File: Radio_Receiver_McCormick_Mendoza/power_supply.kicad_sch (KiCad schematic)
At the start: 31 parts, among them J1 VBAT, J2 GND, J23 VDDA, J26 +5V, J3 VA_3.3, J36 +5V RAW, J37 V_4.5, J39 VDD, J4 VA_4.5, J6 Conn_01x02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

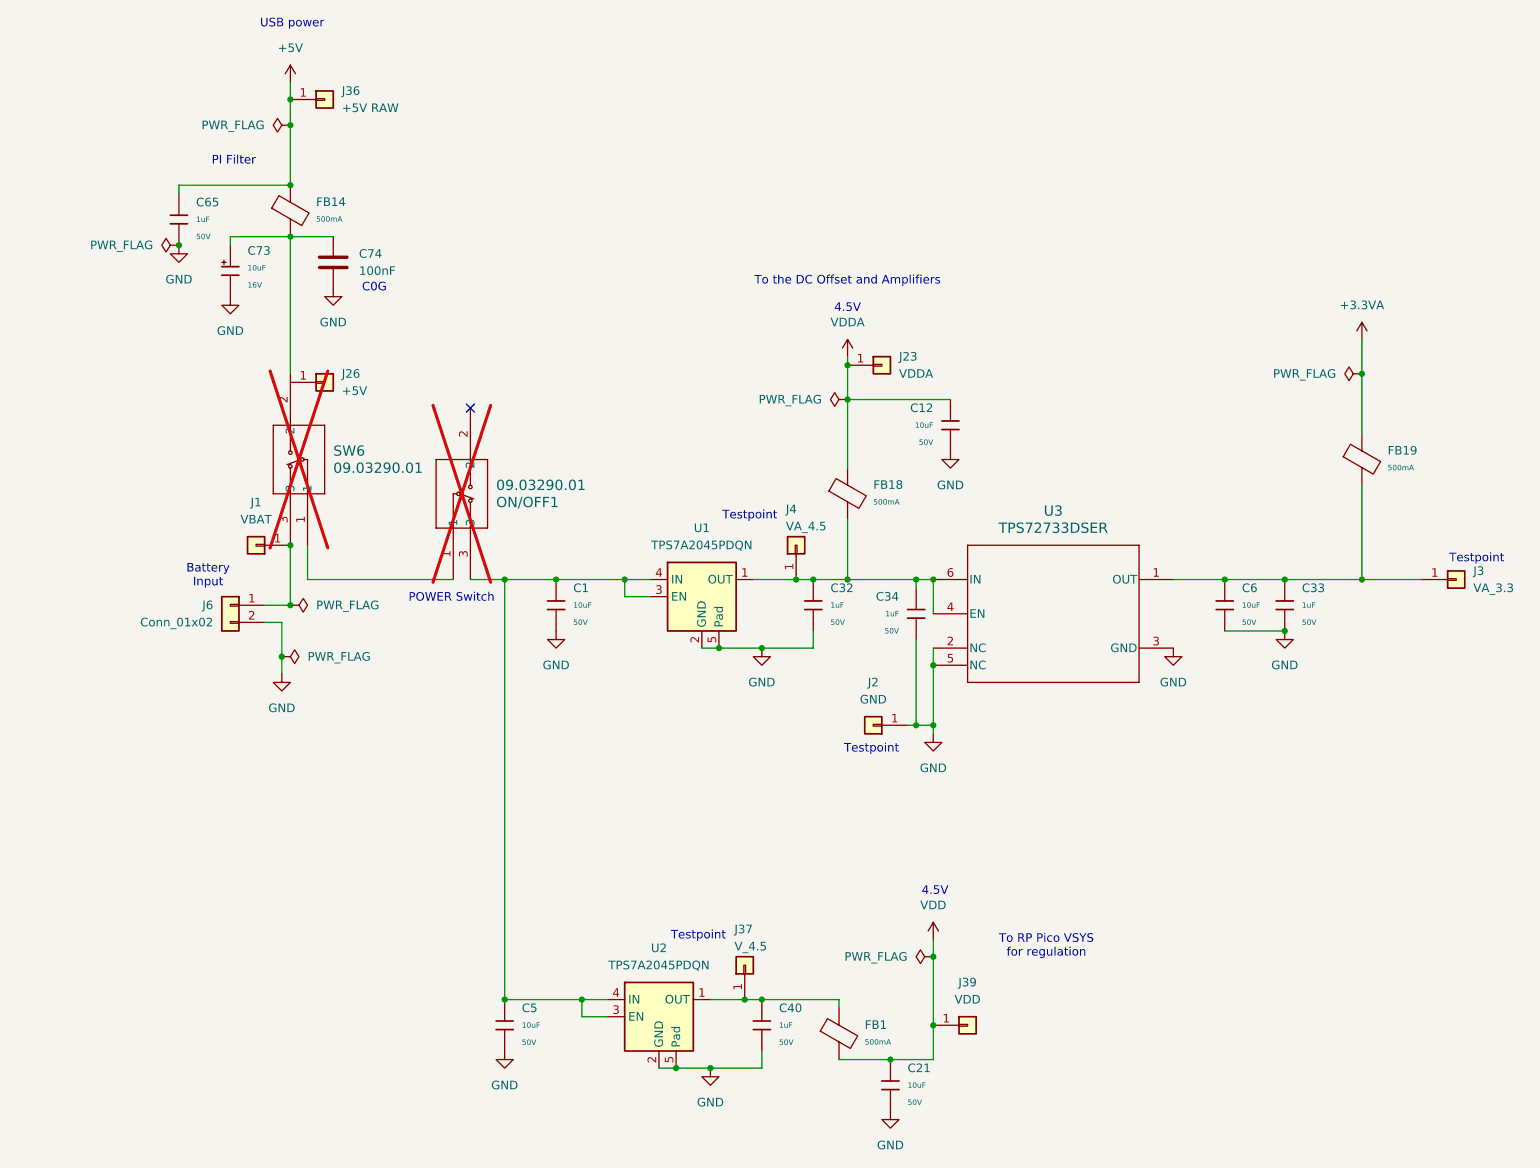
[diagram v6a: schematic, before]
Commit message: Arranged power components on PCB
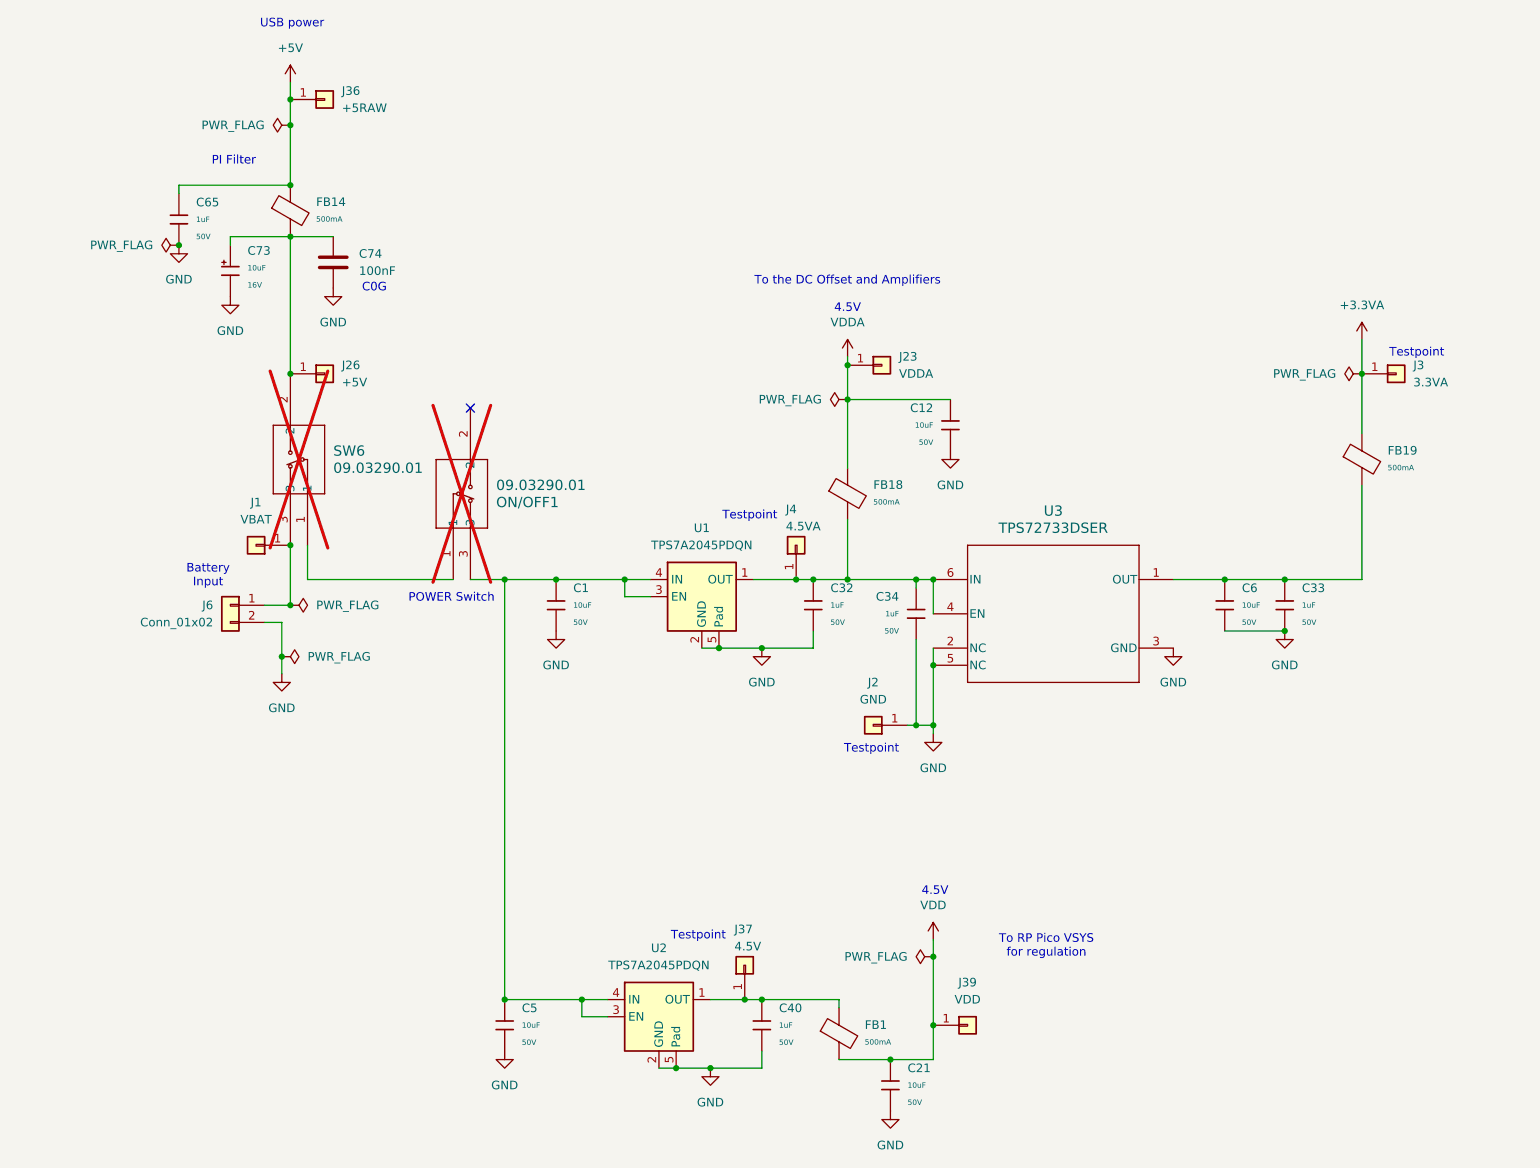
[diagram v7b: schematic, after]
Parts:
- J3: value VA_3.3 -> 3.3VA
- J36: value +5V RAW -> +5RAW
- J37: value V_4.5 -> 4.5V
- J4: value VA_4.5 -> 4.5VA
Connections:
- net +3.3VA: now also J3.1 (Pin_1)
- net at C73.1, C74.1, FB14.2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: now also J26.1 (Pin_1)
- net at C33.1, C6.1, FB19.2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: no longer J3.1 (Pin_1)
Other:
- moved on the sheet: J26, J3
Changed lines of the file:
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@@
 	(text "Testpoint"
 		(exclude_from_sim no)
-		(at 235.458 98.552 0)
+		(at 226.568 68.072 0)
 		(effects
 			(font
@@
 	)
 	(junction
-		(at 218.44 101.6)
-		(diameter 0)
-		(color 0 0 0 0)
-	)
-	(junction
 		(at 59.69 105.41)
 		(diameter 0)
@@
 	)
 	(junction
+		(at 59.69 71.12)
+		(diameter 0)
+		(color 0 0 0 0)
+	)
+	(junction
 		(at 59.69 34.29)
 		(diameter 0)
@@
 	(wire
 		(pts
-			(xy 218.44 101.6) (xy 227.33 101.6)
-		)
-		(stroke
-			(width 0)
-			(type default)
-		)
-	)
-	(wire
-		(pts
 			(xy 154.94 101.6) (xy 154.94 106.68)
 		)
@@
 	(symbol
 		(lib_id "Connector_Generic:Conn_01x01")
-		(at 64.77 72.39 0)
+		(at 64.77 71.12 0)
 		(unit 1)
 		(body_style 1)
@@
 		(fields_autoplaced yes)
 		(property "Reference" "J26"
-			(at 67.31 71.1199 0)
+			(at 67.31 69.8499 0)
 			(show_name no)
 			(do_not_autoplace no)
@@
 		)
 		(property "Value" "+5V"
-			(at 67.31 73.6599 0)
+			(at 67.31 72.3899 0)
 			(show_name no)
 			(do_not_autoplace no)
@@
 		)
 		(property "Footprint" "Connector_PinHeader_2.54mm:PinHeader_1x01_P2.54mm_Vertical"
-			(at 64.77 72.39 0)
+			(at 64.77 71.12 0)
 			(hide yes)
 			(show_name no)
@@
 		)
 		(property "Datasheet" ""
-			(at 64.77 72.39 0)
+			(at 64.77 71.12 0)
 			(hide yes)
 			(show_name no)
@@
 		)
 		(property "Description" "Generic connector, single row, 01x01, script generated (kicad-library-utils/schlib/autogen/connector/)"
-			(at 64.77 72.39 0)
+			(at 64.77 71.12 0)
 			(hide yes)
 			(show_name no)
@@
 			)
 		)
-		(property "Value" "+5V RAW"
+		(property "Value" "+5RAW"
 			(at 67.31 31.7499 0)
 			(show_name no)
@@
 	(symbol
 		(lib_id "Connector_Generic:Conn_01x01")
-		(at 232.41 101.6 0)
+		(at 223.52 71.12 0)
 		(unit 1)
 		(body_style 1)
@@
 		(fields_autoplaced yes)
 		(property "Reference" "J3"
-			(at 234.95 100.3299 0)
+			(at 226.06 69.8499 0)
 			(show_name no)
 			(do_not_autoplace no)
@@
 			)
 		)
-		(property "Value" "VA_3.3"
-			(at 234.95 102.8699 0)
+		(property "Value" "3.3VA"
+			(at 226.06 72.3899 0)
 			(show_name no)
 			(do_not_autoplace no)
@@
 		)
 		(property "Footprint" "Connector_PinHeader_2.54mm:PinHeader_1x01_P2.54mm_Vertical"
-			(at 232.41 101.6 0)
+			(at 223.52 71.12 0)
 			(hide yes)
 			(show_name no)
@@
 		)
 		(property "Datasheet" ""
-			(at 232.41 101.6 0)
+			(at 223.52 71.12 0)
 			(hide yes)
 			(show_name no)
@@
 		)
 		(property "Description" "Generic connector, single row, 01x01, script generated (kicad-library-utils/schlib/autogen/connector/)"
-			(at 232.41 101.6 0)
+			(at 223.52 71.12 0)
 			(hide yes)
 			(show_name no)
@@
 			)
 		)
-		(property "Value" "V_4.5"
+		(property "Value" "4.5V"
 			(at 125.476 155.956 90)
 			(show_name no)
@@
 			)
 		)
-		(property "Value" "VA_4.5"
+		(property "Value" "4.5VA"
 			(at 133.096 93.726 90)
 			(show_name no)

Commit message: Routed antenna and isolated GNDA
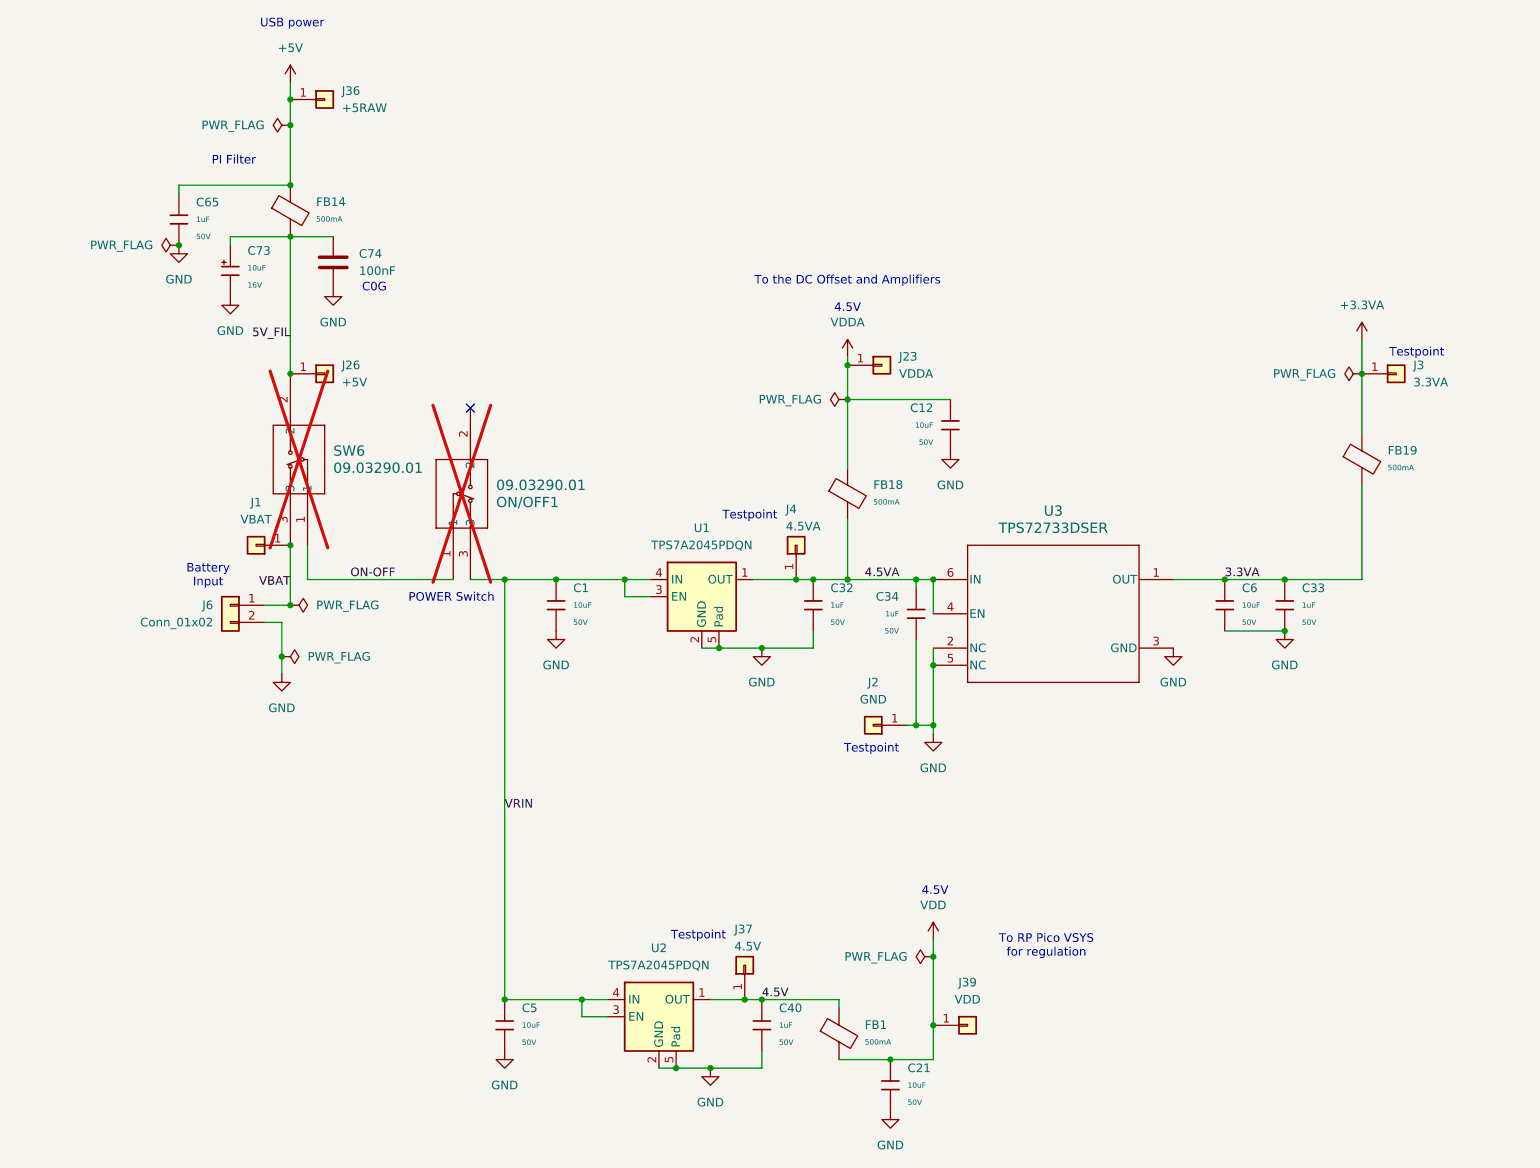
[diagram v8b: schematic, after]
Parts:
- U3: footprint TPS727-3.3V_regulator:DSE0006A -> Reciever_Parts:TS727_3.3VDSE0006A
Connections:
- net 5V_FIL: now reaches C73.1, C74.1, FB14.2, J26.1 (Pin_1), SW6.2
- net VRIN: now reaches C1.1, C5.1, ON/OFF1.3, U1.3 (EN), U1.4 (IN), U2.3 (EN), U2.4 (IN)
- net 4.5V: now reaches C40.1, FB1.1, J37.1 (Pin_1), U2.1 (OUT)
- net VBAT: now reaches J1.1 (Pin_1), J6.1 (Pin_1), SW6.3
- net 4.5VA: now reaches C32.1, C34.2, FB18.2, J4.1 (Pin_1), U1.1 (OUT), U3.4 (EN), U3.6 (IN)
- net ON-OFF: now reaches ON/OFF1.1, SW6.1
- net 3.3VA: now reaches C33.1, C6.1, FB19.2, U3.1 (OUT)
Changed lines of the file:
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@@
 		)
 	)
+	(label "4.5VA"
+		(at 144.78 101.6 0)
+		(effects
+			(font
+				(size 1.27 1.27)
+			)
+			(justify left bottom)
+		)
+	)
+	(label "ON-OFF"
+		(at 68.58 101.6 0)
+		(effects
+			(font
+				(size 1.27 1.27)
+			)
+			(justify left bottom)
+		)
+	)
+	(label "4.5V"
+		(at 129.54 163.83 0)
+		(effects
+			(font
+				(size 1.27 1.27)
+			)
+			(justify left bottom)
+		)
+	)
+	(label "VRIN"
+		(at 91.44 135.89 0)
+		(effects
+			(font
+				(size 1.27 1.27)
+			)
+			(justify left bottom)
+		)
+	)
+	(label "3.3VA"
+		(at 198.12 101.6 0)
+		(effects
+			(font
+				(size 1.27 1.27)
+			)
+			(justify left bottom)
+		)
+	)
+	(label "5V_FIL"
+		(at 59.69 66.04 180)
+		(effects
+			(font
+				(size 1.27 1.27)
+			)
+			(justify right bottom)
+		)
+	)
+	(label "VBAT"
+		(at 59.69 102.87 180)
+		(effects
+			(font
+				(size 1.27 1.27)
+			)
+			(justify right bottom)
+		)
+	)
 	(symbol
 		(lib_id "PCM_JLCPCB-Inductors:Ferrite,0805,(2)")
@@
 			)
 		)
-		(property "Footprint" "TPS727-3.3V_regulator:DSE0006A"
+		(property "Footprint" "Reciever_Parts:TS727_3.3VDSE0006A"
 			(at 172.72 106.68 0)
 			(hide yes)
